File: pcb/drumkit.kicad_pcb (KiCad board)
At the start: 2 copper layers, 26 parts, among them J1 BATTERY, J2 Conn_01x04_Female, SW1 BUTTON1, SW2 BUTTON2, SW3 BUTTON3, SW4 BUTTON4, SW5 POWER_SW, U1 Pico

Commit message: why is it not updating?
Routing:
- net GND: track 360.1 -> 361.1 mm
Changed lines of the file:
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@@
   (segment (start 154.265 60.06) (end 154.265 53.716877) (width 2) (layer "B.Cu") (net 8))
   (segment (start 174.625 104.14) (end 174.625 107.155) (width 1) (layer "B.Cu") (net 8))
+  (segment (start 142.875 107.315) (end 142.875 99.695) (width 1) (layer "B.Cu") (net 8))
   (segment (start 176.946877 53.975) (end 177.8 53.121877) (width 2) (layer "B.Cu") (net 8))
-  (segment (start 142.875 99.695) (end 142.875 106.33) (width 1) (layer "B.Cu") (net 8))
   (segment (start 155.575 106.84) (end 156.05 107.315) (width 1) (layer "B.Cu") (net 8))
   (segment (start 160.528 50.927) (end 163.576 53.975) (width 2) (layer "B.Cu") (net 8))

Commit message: cleanup pcb
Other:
- board outline added: 118.7 x 90.8 mm
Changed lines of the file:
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@@
   )
   (paper "A4")
+  (title_block
+    (title "Drumkit")
+    (date "2024-03-25")
+    (rev "1")
+  )
   (layers
     (0 "F.Cu" signal)
@@
   (gr_circle (center 201.93 20.32) (end 203.2 20.32)
     (stroke (width 0.2) (type default)) (fill none) (layer "B.Cu"))
-  (gr_rect (start 85.09 18.415) (end 203.835 109.22)
-    (stroke (width 0.2) (type default)) (fill none) (layer "B.Cu"))
   (gr_circle (center 201.93 107.315) (end 203.2 106.68)
     (stroke (width 0.2) (type default)) (fill none) (layer "B.Cu"))
   (gr_circle (center 86.995 20.32) (end 88.265 20.32)
     (stroke (width 0.2) (type default)) (fill none) (layer "B.Cu"))
+  (gr_rect (start 85.09 18.415) (end 203.835 109.22)
+    (stroke (width 0.2) (type default)) (fill none) (layer "Edge.Cuts"))
   (segment (start 139.065 90.805) (end 142.875 94.615) (width 1) (layer "B.Cu") (net 1))
   (segment (start 133.35 90.805) (end 139.065 90.805) (width 1) (layer "B.Cu") (net 1))

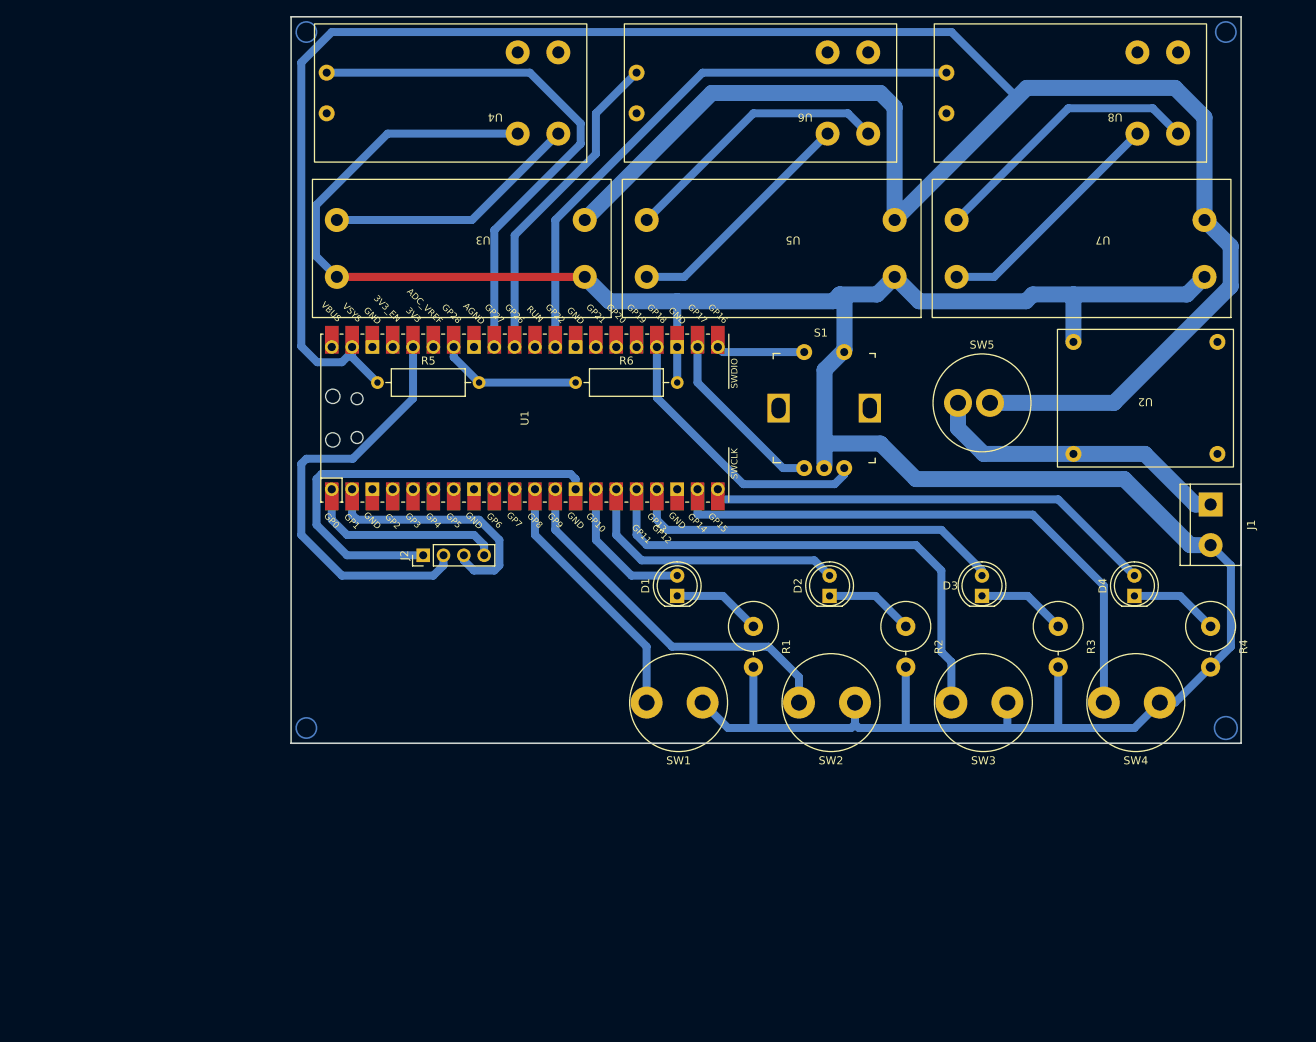
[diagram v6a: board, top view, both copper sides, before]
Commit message: cleanup strange connection in schematic and pcb
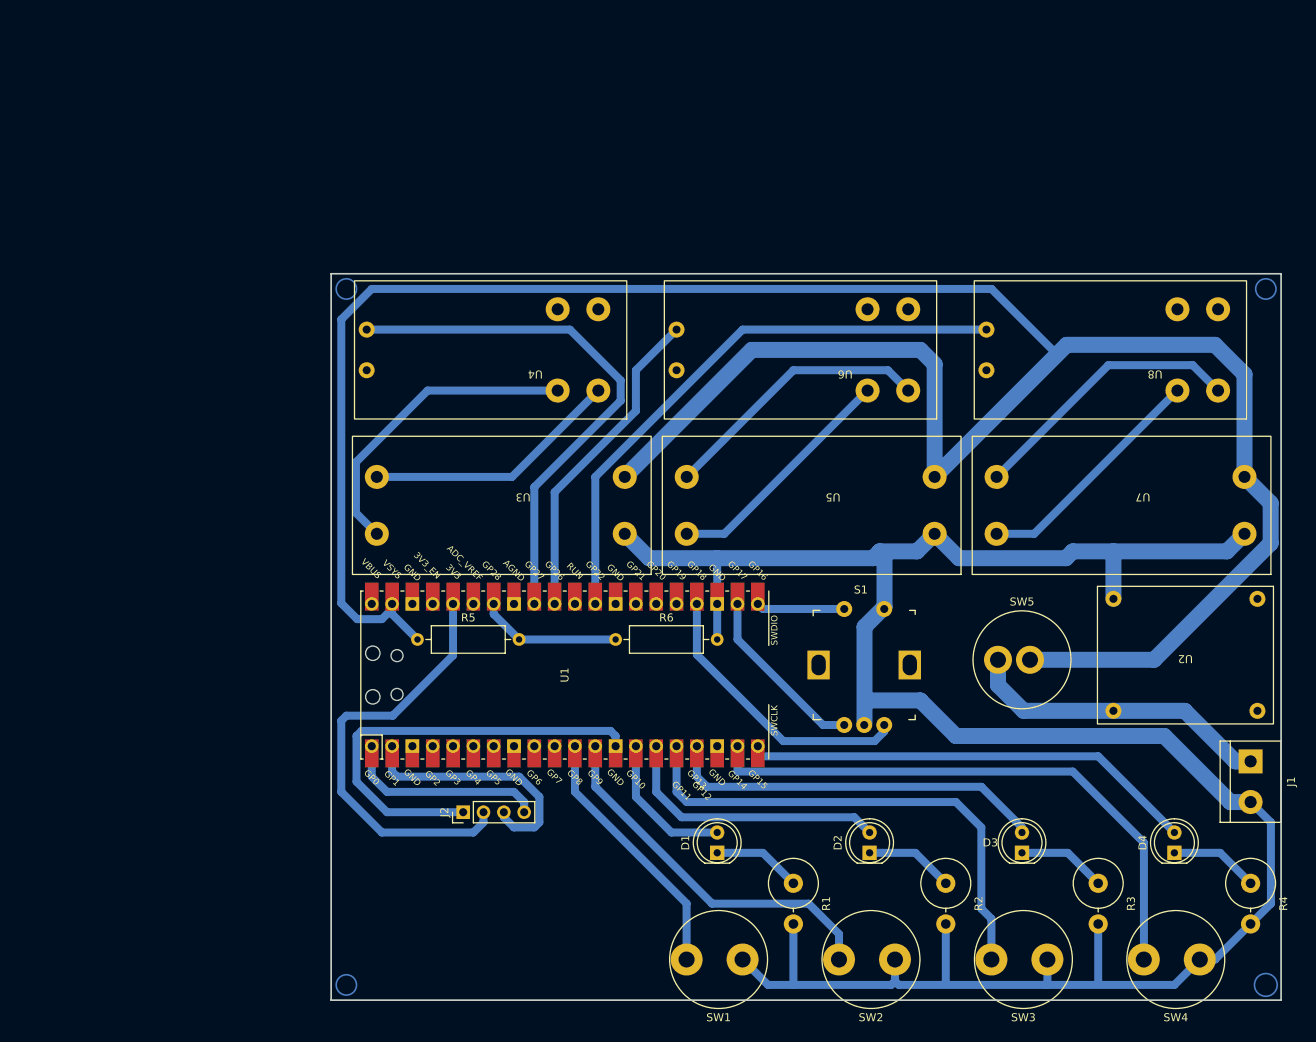
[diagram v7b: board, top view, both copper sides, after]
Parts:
- moved J2 32.5 mm to (106.6, 117.8)
- moved R1 32.5 mm to (147.9, 126.7)
- moved R2 32.5 mm to (166.9, 126.7)
- moved R3 32.5 mm to (186.0, 126.7)
- moved R4 32.5 mm to (205.0, 126.7)
- moved SW5 32.5 mm to (173.4, 98.8)
- moved U3 32.5 mm to (114.1, 78.0)
- moved U5 32.5 mm to (152.8, 78.0)
- moved U7 32.5 mm to (191.6, 78.0)
- moved D1 32.5 mm to (138.3, 122.9)
- moved D2 32.5 mm to (157.4, 122.9)
- moved D3 32.5 mm to (176.4, 122.9)
- moved D4 32.5 mm to (195.5, 122.9)
- moved J1 32.5 mm to (205.0, 111.5)
- moved R5 32.5 mm to (100.9, 96.2)
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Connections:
- U3 pad 3: GND -> Net-(U3-Out-)
- U4 pad 2: GND -> Net-(U3-Out-)
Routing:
- net GND: track 361.1 -> 291.1 mm
- net Net-(U3-Out-): track 0.00 -> 39.0 mm
